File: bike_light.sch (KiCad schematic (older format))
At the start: 0 parts

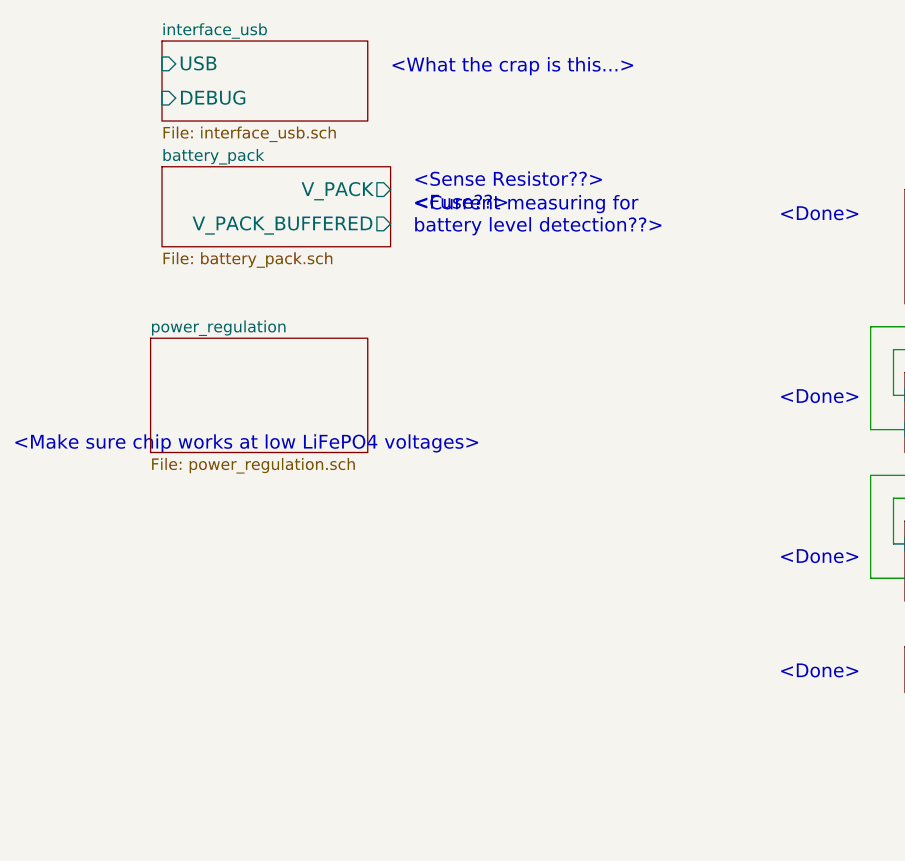
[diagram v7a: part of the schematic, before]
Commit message: completed USB comm circuits
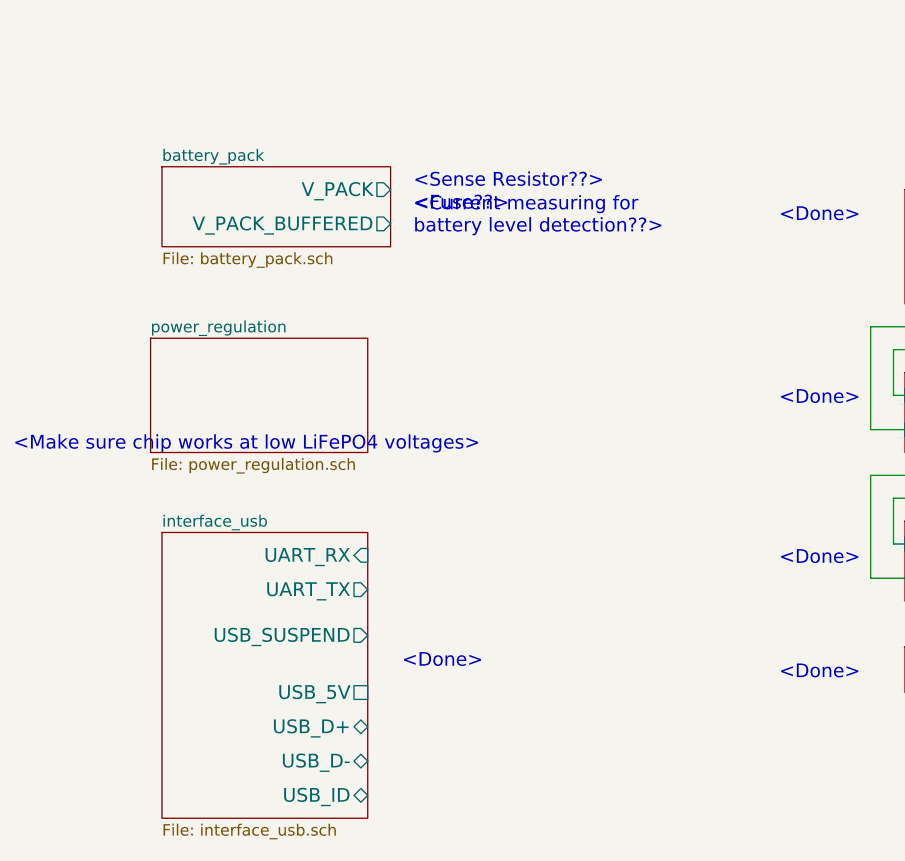
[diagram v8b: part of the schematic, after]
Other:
- note removed: "<What the crap is this...>"
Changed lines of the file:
@@
 $EndSheet
 $Sheet
-S 1250 1100 900  350
+S 1250 3250 900  1250
 U 5224C595
 F0 "interface_usb" 50
 F1 "interface_usb.sch" 50
-F2 "USB" I L 1250 1200 60
-F3 "DEBUG" I L 1250 1350 60
+F2 "UART_RX" I R 2150 3350 60
+F3 "UART_TX" O R 2150 3500 60
+F4 "USB_SUSPEND" O R 2150 3700 60
+F5 "USB_5V" U R 2150 3950 60
+F6 "USB_D+" B R 2150 4100 60
+F7 "USB_D-" B R 2150 4250 60
+F8 "USB_ID" B R 2150 4400 60
 $EndSheet
 $Sheet
@@
 Text Notes 2350 1950 0    60   ~ 0
 <Current measuring for \nbattery level detection??>
-Text Notes 2250 1250 0    60   ~ 0
-<What the crap is this...>
+Text Notes 2300 3850 0    60   ~ 0
+<Done>
 Text Notes 600  2900 0    60   ~ 0
 <Make sure chip works at low LiFePO4 voltages>
